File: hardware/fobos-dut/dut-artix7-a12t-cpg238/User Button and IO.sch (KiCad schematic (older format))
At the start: 22 parts, among them Q4 BSS138, Q5 BSS138, Q6 BSS138, Q7 BSS138

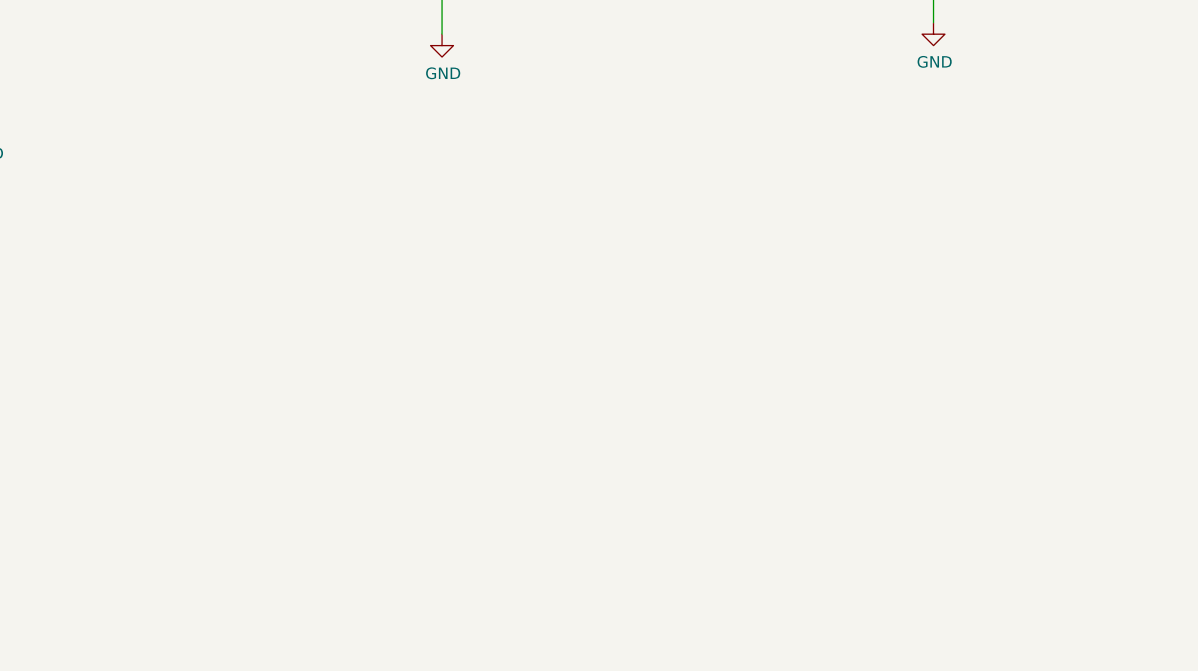
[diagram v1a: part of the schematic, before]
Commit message: Connected the fixed signals to the FPGA, flexible IO are left unconnected Added 0.1 ohm resistors to the 1V8 and 3V3 power rails, added test points which allow for easy measurement Updated ARTIX7-A12T-CPG238 symbol to make schematic route similarly to the last symbol Connected CFGVBS signal to the 3V3 rail, was previously connected to VCCINT which was a mistake Ran through 7 Series schematic review checklist - 7_Series_Schematic_Review_Recommendations.xlsm Added Xilinx pinout files for the CPG238 package Generated schematic for the csg325 for easy referencing
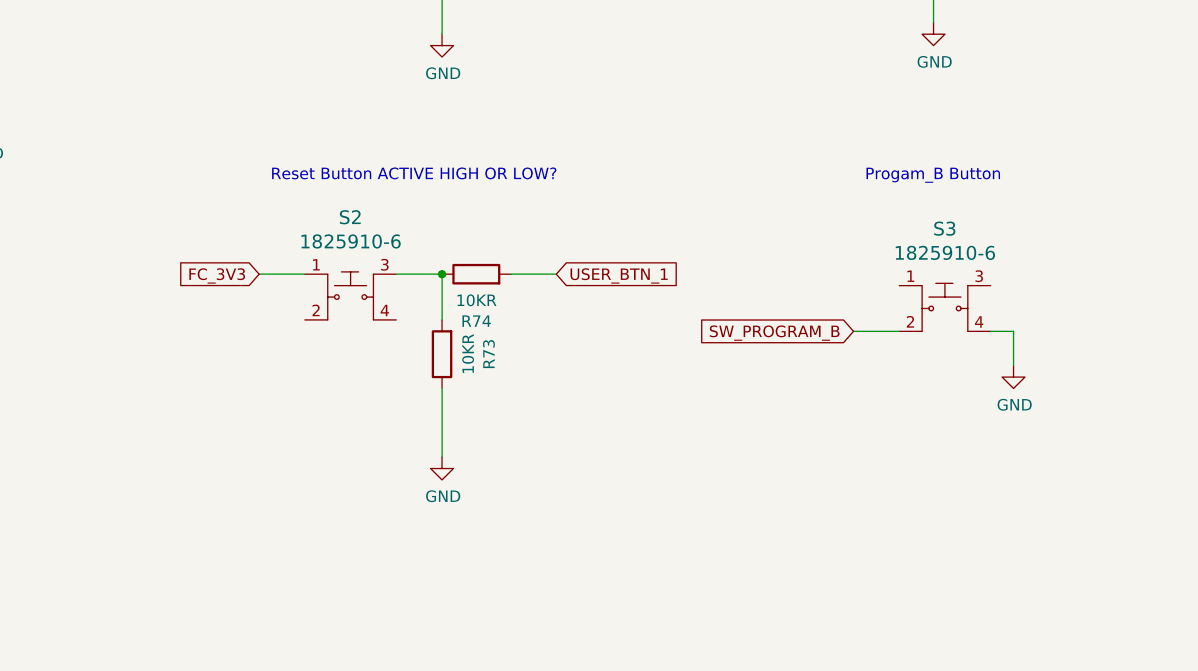
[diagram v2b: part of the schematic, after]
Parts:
- added R73, R74: 10KR, Resistor_SMD:R_0603_1608Metric, symbol Device:R
- added S2, S3: 1825910-6, cerg:Switch_Tactile_THT_6x6mm, symbol cerg:1825910-6
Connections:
- net labels added: SW_PROGRAM_B
- wire segments 62 -> 70
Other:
- note added: "Progam_B Button"
- note added: "Reset Button ACTIVE HIGH OR LOW?"
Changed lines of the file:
@@
 $Descr A4 11693 8268
 encoding utf-8
-Sheet 7 8
+Sheet 6 8
 Title ""
 Date ""
@@
 	1    0    0    -1
 $EndComp
+Text Notes 7200 4150 0    50   ~ 0
+Reset Button ACTIVE HIGH OR LOW?
+$Comp
+L Device:R R?
+U 1 1 60EF3D05
+P 7950 4900
+AR Path="/5F449901/60EF3D05" Ref="R?"  Part="1"
+AR Path="/600CE672/60EF3D05" Ref="R73"  Part="1"
+F 0 "R73" V 7743 4900 50  0000 C CNN
+F 1 "10KR" V 7834 4900 50  0000 C CNN
+F 2 "Resistor_SMD:R_0603_1608Metric" V 7880 4900 50  0001 C CNN
+F 3 "~" H 7950 4900 50  0001 C CNN
+F 4 "RES SMD 10K OHM 1% 1/10W 0603" H 7950 4900 50  0001 C CNN "Description"
+F 5 "ERJ-3EKF1002V" H 7950 4900 50  0001 C CNN "MPN"
+F 6 "Panasonic Electronic Components" H 7950 4900 50  0001 C CNN "Manufacturer"
+	1    7950 4900
+	-1   0    0    1
+$EndComp
+$Comp
+L Device:R R?
+U 1 1 60EF3D0E
+P 8100 4550
+AR Path="/5F449901/60EF3D0E" Ref="R?"  Part="1"
+AR Path="/600CE672/60EF3D0E" Ref="R74"  Part="1"
+F 0 "R74" V 7893 4550 50  0000 C CNN
+F 1 "10KR" V 7984 4550 50  0000 C CNN
+F 2 "Resistor_SMD:R_0603_1608Metric" V 8030 4550 50  0001 C CNN
+F 3 "~" H 8100 4550 50  0001 C CNN
+F 4 "RES SMD 10K OHM 1% 1/10W 0603" H 8100 4550 50  0001 C CNN "Description"
+F 5 "ERJ-3EKF1002V" H 8100 4550 50  0001 C CNN "MPN"
+F 6 "Panasonic Electronic Components" H 8100 4550 50  0001 C CNN "Manufacturer"
+	1    8100 4550
+	0    -1   -1   0
+$EndComp
+Wire Wire Line
+	7750 4550 7950 4550
+Wire Wire Line
+	7950 4750 7950 4550
+Connection ~ 7950 4550
+$Comp
+L power:GND #PWR?
+U 1 1 60EF3D17
+P 7950 5350
+AR Path="/5F449901/60EF3D17" Ref="#PWR?"  Part="1"
+AR Path="/600CE672/60EF3D17" Ref="#PWR033"  Part="1"
+F 0 "#PWR033" H 7950 5100 50  0001 C CNN
+F 1 "GND" H 7955 5177 50  0000 C CNN
+F 2 "" H 7950 5350 50  0001 C CNN
+F 3 "" H 7950 5350 50  0001 C CNN
+	1    7950 5350
+	1    0    0    -1
+$EndComp
+Wire Wire Line
+	7950 5050 7950 5350
+Text GLabel 7150 4550 0    50   Input ~ 0
+FC_3V3
+Wire Wire Line
+	7150 4550 7350 4550
+Text GLabel 8450 4550 2    50   Input ~ 0
+USER_BTN_1
+Wire Wire Line
+	8450 4550 8250 4550
+$Comp
+L cerg:1825910-6 S2
+U 1 1 60EF3D2B
+P 7550 4650
+F 0 "S2" H 7550 4997 60  0000 C CNN
+F 1 "1825910-6" H 7550 4891 60  0000 C CNN
+F 2 "cerg:Switch_Tactile_THT_6x6mm" H 7750 4850 60  0001 L CNN
+F 3 "https://www.te.com/commerce/DocumentDelivery/DDEController?Action=srchrtrv&DocNm=1825910&DocType=Customer+Drawing&DocLang=English" H 7750 4950 60  0001 L CNN
+F 4 "450-1650-ND" H 7750 5050 60  0001 L CNN "Digi-Key_PN"
+F 5 "1825910-6" H 7750 5150 60  0001 L CNN "MPN"
+F 6 "Switches" H 7750 5250 60  0001 L CNN "Category"
+F 7 "Tactile Switches" H 7750 5350 60  0001 L CNN "Family"
+F 8 "https://www.te.com/commerce/DocumentDelivery/DDEController?Action=srchrtrv&DocNm=1825910&DocType=Customer+Drawing&DocLang=English" H 7750 5450 60  0001 L CNN "DK_Datasheet_Link"
+F 9 "/product-detail/en/te-connectivity-alcoswitch-switches/1825910-6/450-1650-ND/1632536" H 7750 5550 60  0001 L CNN "DK_Detail_Page"
+F 10 "SWITCH TACTILE SPST-NO 0.05A 24V" H 7750 5650 60  0001 L CNN "Description"
+F 11 "TE Connectivity ALCOSWITCH Switches" H 7750 5750 60  0001 L CNN "Manufacturer"
+F 12 "Active" H 7750 5850 60  0001 L CNN "Status"
+	1    7550 4650
+	1    0    0    -1
+$EndComp
+$Comp
+L power:GND #PWR?
+U 1 1 60FBBA52
+P 10450 4950
+AR Path="/5F3A1954/60FBBA52" Ref="#PWR?"  Part="1"
+AR Path="/600CE672/60FBBA52" Ref="#PWR034"  Part="1"
+F 0 "#PWR034" H 10450 4700 50  0001 C CNN
+F 1 "GND" H 10455 4777 50  0000 C CNN
+F 2 "" H 10450 4950 50  0001 C CNN
+F 3 "" H 10450 4950 50  0001 C CNN
+	1    10450 4950
+	1    0    0    -1
+$EndComp
+Text GLabel 9750 4800 0    50   Input ~ 0
+SW_PROGRAM_B
+Wire Wire Line
+	10350 4800 10450 4800
+Wire Wire Line
+	10450 4800 10450 4950
+Wire Wire Line
+	9950 4800 9750 4800
+$Comp
+L cerg:1825910-6 S?
+U 1 1 60FBBA65
+P 10150 4700
+AR Path="/5F3A1954/60FBBA65" Ref="S?"  Part="1"
+AR Path="/600CE672/60FBBA65" Ref="S3"  Part="1"
+F 0 "S3" H 10150 5047 60  0000 C CNN
+F 1 "1825910-6" H 10150 4941 60  0000 C CNN
+F 2 "cerg:Switch_Tactile_THT_6x6mm" H 10350 4900 60  0001 L CNN
+F 3 "https://www.te.com/commerce/DocumentDelivery/DDEController?Action=srchrtrv&DocNm=1825910&DocType=Customer+Drawing&DocLang=English" H 10350 5000 60  0001 L CNN
+F 4 "450-1650-ND" H 10350 5100 60  0001 L CNN "Digi-Key_PN"
+F 5 "1825910-6" H 10350 5200 60  0001 L CNN "MPN"
+F 6 "Switches" H 10350 5300 60  0001 L CNN "Category"
+F 7 "Tactile Switches" H 10350 5400 60  0001 L CNN "Family"
+F 8 "https://www.te.com/commerce/DocumentDelivery/DDEController?Action=srchrtrv&DocNm=1825910&DocType=Customer+Drawing&DocLang=English" H 10350 5500 60  0001 L CNN "DK_Datasheet_Link"
+F 9 "/product-detail/en/te-connectivity-alcoswitch-switches/1825910-6/450-1650-ND/1632536" H 10350 5600 60  0001 L CNN "DK_Detail_Page"
+F 10 "SWITCH TACTILE SPST-NO 0.05A 24V" H 10350 5700 60  0001 L CNN "Description"
+F 11 "TE Connectivity ALCOSWITCH Switches" H 10350 5800 60  0001 L CNN "Manufacturer"
+F 12 "Active" H 10350 5900 60  0001 L CNN "Status"
+	1    10150 4700
+	1    0    0    -1
+$EndComp
+Text Notes 9800 4150 0    50   ~ 0
+Progam_B Button
 $EndSCHEMATC

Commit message: Added SMA-JOHNSON-142-0701-201 Vertical SMA footprint to CERG lib, added this footprint to the Vcore measurement Re-positioned Power circuitry to the top right quadrant Re-positioned FOBOS connector to the center on the left edge of the board Re-positioned JTAG Connector, Mode switch, and gain control switch to the top left quadrant of the board
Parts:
- D2, D3, D4: symbol dk_LED-Indication-Discrete:LG_L29K-G2J1-24-Z -> Device:LED
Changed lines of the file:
@@
 $EndComp
 $Comp
-L dk_LED-Indication-Discrete:LG_L29K-G2J1-24-Z D?
+L Device:LED D?
 U 1 1 600D00D8
-P 2050 2250
+P 2050 2200
 AR Path="/5F449901/600D00D8" Ref="D?"  Part="1"
 AR Path="/600CE672/600D00D8" Ref="D2"  Part="1"
-F 0 "D2" V 1947 2428 60  0000 L CNN
-F 1 "LG_L29K-G2J1-24-Z" V 2053 2428 60  0001 L CNN
-F 2 "LED_SMD:LED_0603_1608Metric" H 2250 2450 60  0001 L CNN
-F 3 "https://dammedia.osram.info/media/resource/hires/osram-dam-2493945/LG%20L29K.pdf" H 2250 2550 60  0001 L CNN
-F 4 "475-2709-1-ND" H 2250 2650 60  0001 L CNN "Digi-Key_PN"
-F 5 "LG L29K-G2J1-24-Z" H 2250 2750 60  0001 L CNN "MPN"
-F 6 "Optoelectronics" H 2250 2850 60  0001 L CNN "Category"
-F 7 "LED Indication - Discrete" H 2250 2950 60  0001 L CNN "Family"
-F 8 "https://dammedia.osram.info/media/resource/hires/osram-dam-2493945/LG%20L29K.pdf" H 2250 3050 60  0001 L CNN "DK_Datasheet_Link"
-F 9 "/product-detail/en/osram-opto-semiconductors-inc/LG-L29K-G2J1-24-Z/475-2709-1-ND/1938876" H 2250 3150 60  0001 L CNN "DK_Detail_Page"
-F 10 "LED GREEN DIFFUSED 0603 SMD" H 2250 3250 60  0001 L CNN "Description"
-F 11 "OSRAM Opto Semiconductors Inc." H 2250 3350 60  0001 L CNN "Manufacturer"
-F 12 "Active" H 2250 3450 60  0001 L CNN "Status"
-	1    2050 2250
-	0    1    1    0
+F 0 "D2" V 1947 2378 60  0000 L CNN
+F 1 "LG_L29K-G2J1-24-Z" V 2053 2378 60  0001 L CNN
+F 2 "LED_SMD:LED_0603_1608Metric" H 2250 2400 60  0001 L CNN
+F 3 "https://dammedia.osram.info/media/resource/hires/osram-dam-2493945/LG%20L29K.pdf" H 2250 2500 60  0001 L CNN
+F 4 "475-2709-1-ND" H 2250 2600 60  0001 L CNN "Digi-Key_PN"
+F 5 "LG L29K-G2J1-24-Z" H 2250 2700 60  0001 L CNN "MPN"
+F 6 "Optoelectronics" H 2250 2800 60  0001 L CNN "Category"
+F 7 "LED Indication - Discrete" H 2250 2900 60  0001 L CNN "Family"
+F 8 "https://dammedia.osram.info/media/resource/hires/osram-dam-2493945/LG%20L29K.pdf" H 2250 3000 60  0001 L CNN "DK_Datasheet_Link"
+F 9 "/product-detail/en/osram-opto-semiconductors-inc/LG-L29K-G2J1-24-Z/475-2709-1-ND/1938876" H 2250 3100 60  0001 L CNN "DK_Detail_Page"
+F 10 "LED GREEN DIFFUSED 0603 SMD" H 2250 3200 60  0001 L CNN "Description"
+F 11 "OSRAM Opto Semiconductors Inc." H 2250 3300 60  0001 L CNN "Manufacturer"
+F 12 "Active" H 2250 3400 60  0001 L CNN "Status"
+	1    2050 2200
+	0    -1   -1   0
 $EndComp
 $Comp
@@
 $EndComp
 $Comp
-L dk_LED-Indication-Discrete:LG_L29K-G2J1-24-Z D?
+L Device:LED D?
 U 1 1 600D0FA2
-P 4100 2300
+P 4100 2250
 AR Path="/5F449901/600D0FA2" Ref="D?"  Part="1"
 AR Path="/600CE672/600D0FA2" Ref="D3"  Part="1"
-F 0 "D3" V 3997 2478 60  0000 L CNN
-F 1 "LG_L29K-G2J1-24-Z" V 4103 2478 60  0001 L CNN
-F 2 "LED_SMD:LED_0603_1608Metric" H 4300 2500 60  0001 L CNN
-F 3 "https://dammedia.osram.info/media/resource/hires/osram-dam-2493945/LG%20L29K.pdf" H 4300 2600 60  0001 L CNN
-F 4 "475-2709-1-ND" H 4300 2700 60  0001 L CNN "Digi-Key_PN"
-F 5 "LG L29K-G2J1-24-Z" H 4300 2800 60  0001 L CNN "MPN"
-F 6 "Optoelectronics" H 4300 2900 60  0001 L CNN "Category"
-F 7 "LED Indication - Discrete" H 4300 3000 60  0001 L CNN "Family"
-F 8 "https://dammedia.osram.info/media/resource/hires/osram-dam-2493945/LG%20L29K.pdf" H 4300 3100 60  0001 L CNN "DK_Datasheet_Link"
-F 9 "/product-detail/en/osram-opto-semiconductors-inc/LG-L29K-G2J1-24-Z/475-2709-1-ND/1938876" H 4300 3200 60  0001 L CNN "DK_Detail_Page"
-F 10 "LED GREEN DIFFUSED 0603 SMD" H 4300 3300 60  0001 L CNN "Description"
-F 11 "OSRAM Opto Semiconductors Inc." H 4300 3400 60  0001 L CNN "Manufacturer"
-F 12 "Active" H 4300 3500 60  0001 L CNN "Status"
-	1    4100 2300
-	0    1    1    0
+F 0 "D3" V 3997 2428 60  0000 L CNN
+F 1 "LG_L29K-G2J1-24-Z" V 4103 2428 60  0001 L CNN
+F 2 "LED_SMD:LED_0603_1608Metric" H 4300 2450 60  0001 L CNN
+F 3 "https://dammedia.osram.info/media/resource/hires/osram-dam-2493945/LG%20L29K.pdf" H 4300 2550 60  0001 L CNN
+F 4 "475-2709-1-ND" H 4300 2650 60  0001 L CNN "Digi-Key_PN"
+F 5 "LG L29K-G2J1-24-Z" H 4300 2750 60  0001 L CNN "MPN"
+F 6 "Optoelectronics" H 4300 2850 60  0001 L CNN "Category"
+F 7 "LED Indication - Discrete" H 4300 2950 60  0001 L CNN "Family"
+F 8 "https://dammedia.osram.info/media/resource/hires/osram-dam-2493945/LG%20L29K.pdf" H 4300 3050 60  0001 L CNN "DK_Datasheet_Link"
+F 9 "/product-detail/en/osram-opto-semiconductors-inc/LG-L29K-G2J1-24-Z/475-2709-1-ND/1938876" H 4300 3150 60  0001 L CNN "DK_Detail_Page"
+F 10 "LED GREEN DIFFUSED 0603 SMD" H 4300 3250 60  0001 L CNN "Description"
+F 11 "OSRAM Opto Semiconductors Inc." H 4300 3350 60  0001 L CNN "Manufacturer"
+F 12 "Active" H 4300 3450 60  0001 L CNN "Status"
+	1    4100 2250
+	0    -1   -1   0
 $EndComp
 $Comp
@@
 $EndComp
 $Comp
-L dk_LED-Indication-Discrete:LG_L29K-G2J1-24-Z D?
+L Device:LED D?
 U 1 1 600D2B6A
-P 5950 2300
+P 5950 2250
 AR Path="/5F449901/600D2B6A" Ref="D?"  Part="1"
 AR Path="/600CE672/600D2B6A" Ref="D4"  Part="1"
-F 0 "D4" V 5847 2478 60  0000 L CNN
-F 1 "LG_L29K-G2J1-24-Z" V 5953 2478 60  0001 L CNN
-F 2 "LED_SMD:LED_0603_1608Metric" H 6150 2500 60  0001 L CNN
-F 3 "https://dammedia.osram.info/media/resource/hires/osram-dam-2493945/LG%20L29K.pdf" H 6150 2600 60  0001 L CNN
-F 4 "475-2709-1-ND" H 6150 2700 60  0001 L CNN "Digi-Key_PN"
-F 5 "LG L29K-G2J1-24-Z" H 6150 2800 60  0001 L CNN "MPN"
-F 6 "Optoelectronics" H 6150 2900 60  0001 L CNN "Category"
-F 7 "LED Indication - Discrete" H 6150 3000 60  0001 L CNN "Family"
-F 8 "https://dammedia.osram.info/media/resource/hires/osram-dam-2493945/LG%20L29K.pdf" H 6150 3100 60  0001 L CNN "DK_Datasheet_Link"
-F 9 "/product-detail/en/osram-opto-semiconductors-inc/LG-L29K-G2J1-24-Z/475-2709-1-ND/1938876" H 6150 3200 60  0001 L CNN "DK_Detail_Page"
-F 10 "LED GREEN DIFFUSED 0603 SMD" H 6150 3300 60  0001 L CNN "Description"
-F 11 "OSRAM Opto Semiconductors Inc." H 6150 3400 60  0001 L CNN "Manufacturer"
-F 12 "Active" H 6150 3500 60  0001 L CNN "Status"
-	1    5950 2300
-	0    1    1    0
+F 0 "D4" V 5847 2428 60  0000 L CNN
+F 1 "LG_L29K-G2J1-24-Z" V 5953 2428 60  0001 L CNN
+F 2 "LED_SMD:LED_0603_1608Metric" H 6150 2450 60  0001 L CNN
+F 3 "https://dammedia.osram.info/media/resource/hires/osram-dam-2493945/LG%20L29K.pdf" H 6150 2550 60  0001 L CNN
+F 4 "475-2709-1-ND" H 6150 2650 60  0001 L CNN "Digi-Key_PN"
+F 5 "LG L29K-G2J1-24-Z" H 6150 2750 60  0001 L CNN "MPN"
+F 6 "Optoelectronics" H 6150 2850 60  0001 L CNN "Category"
+F 7 "LED Indication - Discrete" H 6150 2950 60  0001 L CNN "Family"
+F 8 "https://dammedia.osram.info/media/resource/hires/osram-dam-2493945/LG%20L29K.pdf" H 6150 3050 60  0001 L CNN "DK_Datasheet_Link"
+F 9 "/product-detail/en/osram-opto-semiconductors-inc/LG-L29K-G2J1-24-Z/475-2709-1-ND/1938876" H 6150 3150 60  0001 L CNN "DK_Detail_Page"
+F 10 "LED GREEN DIFFUSED 0603 SMD" H 6150 3250 60  0001 L CNN "Description"
+F 11 "OSRAM Opto Semiconductors Inc." H 6150 3350 60  0001 L CNN "Manufacturer"
+F 12 "Active" H 6150 3450 60  0001 L CNN "Status"
+	1    5950 2250
+	0    -1   -1   0
 $EndComp
 $Comp

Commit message: updated library ref for diode and FET, placed target connector and some parts
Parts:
- D5: symbol dk_LED-Indication-Discrete:LG_L29K-G2J1-24-Z -> Device:LED
- Q4, Q5, Q6: symbol Transistor:BSS138 -> Transistor_FET:BSS138
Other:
- note added: "Isn't this LED pointing the wrong way?"
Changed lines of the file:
@@
 $EndComp
 $Comp
-L dk_LED-Indication-Discrete:LG_L29K-G2J1-24-Z D?
+L Device:LED D?
 U 1 1 602D02FE
 P 2050 4750
@@
 $EndComp
 $Comp
-L Transistor:BSS138 Q5
+L Transistor_FET:BSS138 Q5
 U 1 1 605337F1
 P 4000 3100
@@
 $EndComp
 $Comp
-L Transistor:BSS138 Q4
+L Transistor_FET:BSS138 Q4
 U 1 1 60535EA9
 P 1950 3050
@@
 $EndComp
 $Comp
-L Transistor:BSS138 Q6
+L Transistor_FET:BSS138 Q6
 U 1 1 60537AA7
 P 1950 5550
@@
 Text Notes 9800 4150 0    50   ~ 0
 Progam_B Button
+Text Notes 2350 4550 0    79   ~ 0
+Isn't this LED pointing the wrong way?
 $EndSCHEMATC
